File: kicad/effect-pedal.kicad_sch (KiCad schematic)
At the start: 50 parts, among them J4 Conn_01x08, J5 Conn_01x09, J6 Conn_01x09, J7 Conn_ARM_JTAG_SWD_10, J8 NJ3FD-V, J9 NJ3FD-V, P2 USB_C_Plug_USB2.0, SW1 RotaryEncoder_Switch, SW2 RotaryEncoder_Switch, SW3 RotaryEncoder_Switch, SW4 RotaryEncoder_Switch, SW5 SW_Push, SW6 SW_SPDT, U1 STM32H723ZGTx, U2 PCM5102A, Y1 Crystal

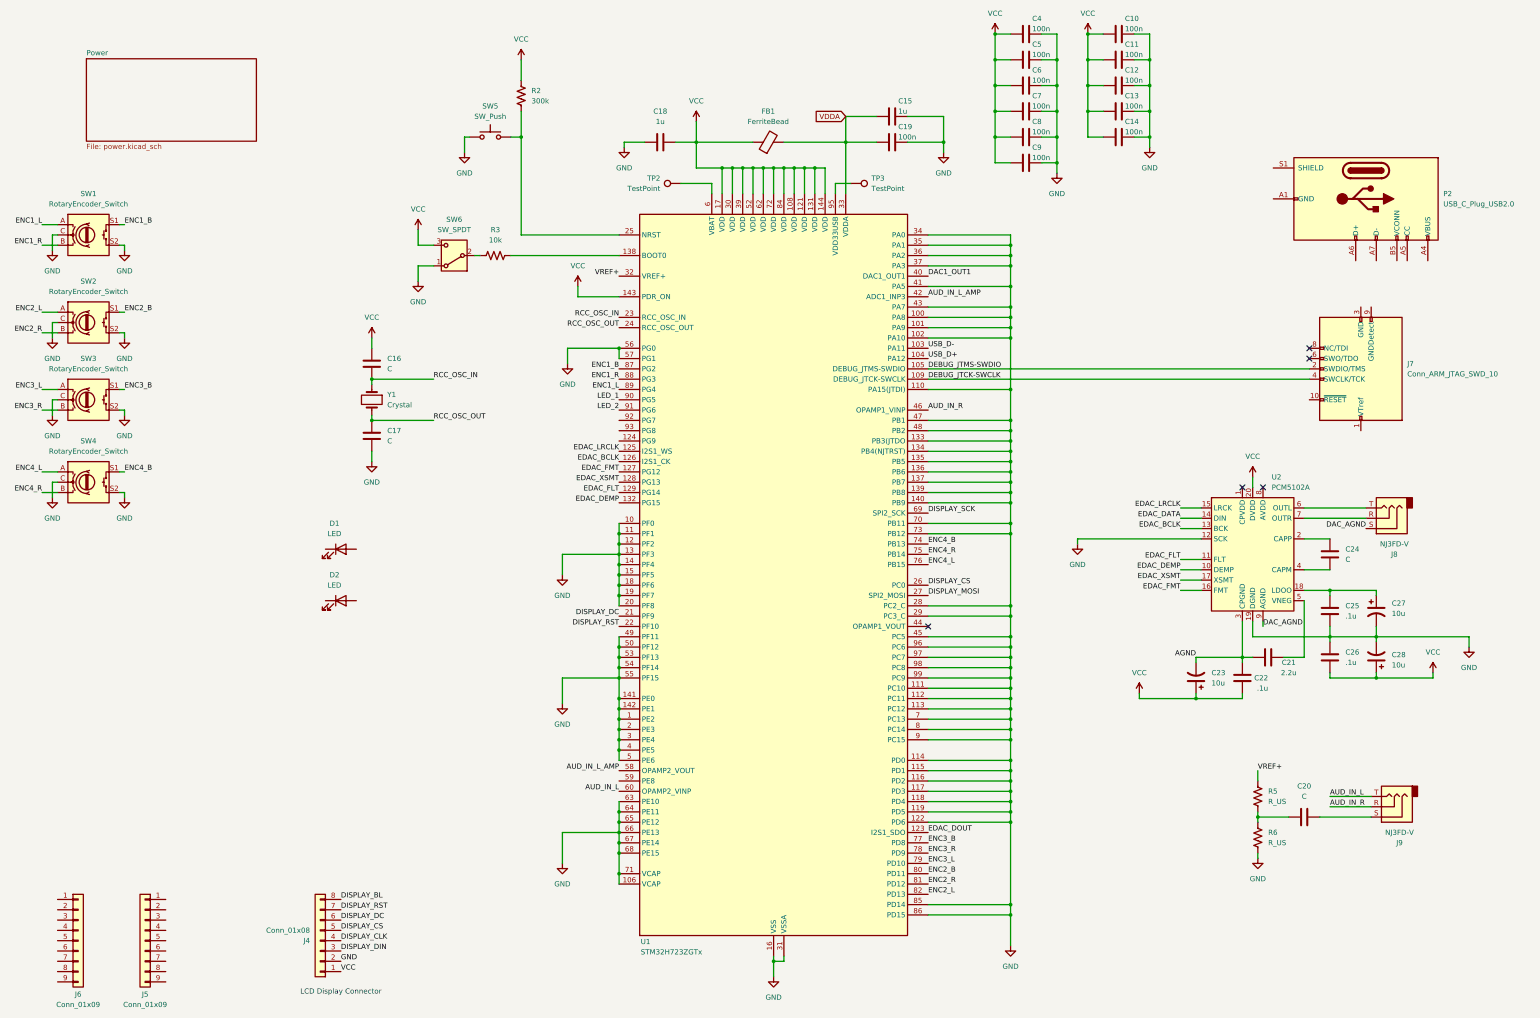
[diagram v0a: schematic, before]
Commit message: Clean up schematic
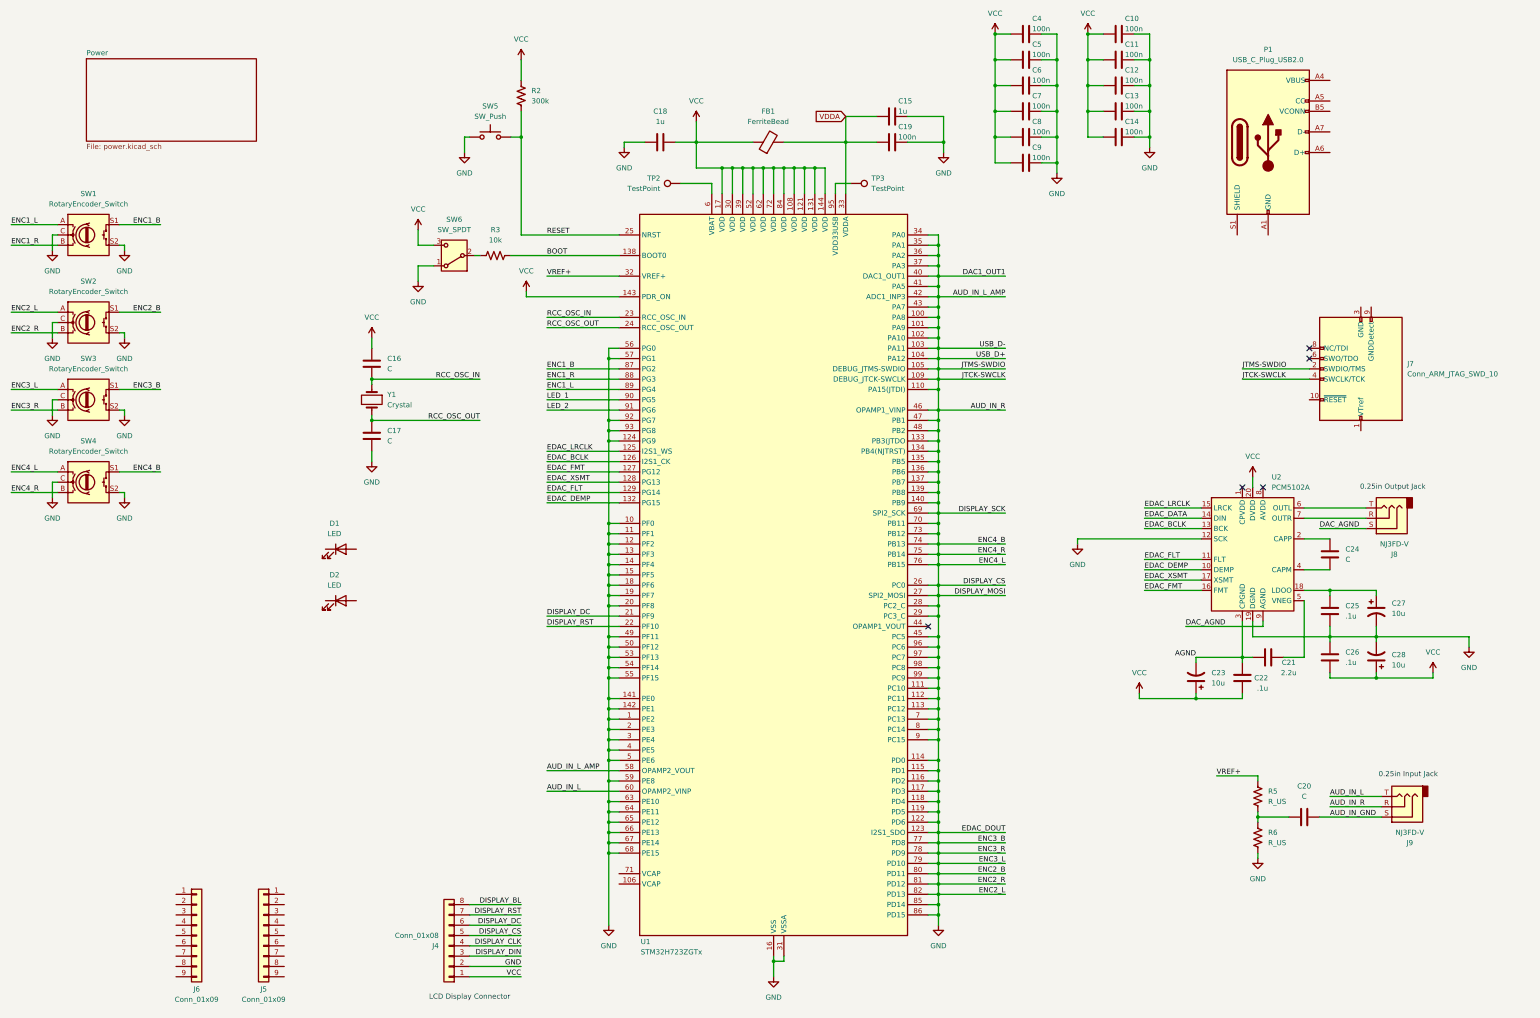
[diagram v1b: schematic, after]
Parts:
- removed P2: USB_C_Plug_USB2.0, symbol Connector:USB_C_Plug_USB2.0
- added P1: USB_C_Plug_USB2.0, symbol Connector:USB_C_Plug_USB2.0
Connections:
- net AUD_IN_L_AMP is gone; now on net GND: U1.42 (PA6), U1.58 (PE7)
- net AUD_IN_R is gone; now on net GND: J9.R, U1.46 (PB0)
- net DAC1_OUT1 is gone; now on net GND: U1.40 (PA4)
- net DEBUG_JTCK-SWCLK is gone; now on net GND: J7.4 (SWCLK/TCK), U1.109 (PA14(JTCK)
- net DEBUG_JTMS-SWDIO is gone; now on net GND: J7.2 (SWDIO/TMS), U1.105 (PA13(JTMS)
- net DISPLAY_CS is gone; now on net GND: J4.5 (Pin_5), U1.26 (PC0)
- net DISPLAY_MOSI is gone; now on net GND: U1.27 (PC1)
- net DISPLAY_SCK is gone; now on net GND: U1.69 (PB10)
- net EDAC_DOUT is gone; now on net GND: U1.123 (PD7)
- net ENC2_B is gone; now on net GND: SW2.S1, U1.80 (PD11)
- net ENC2_L is gone; now on net GND: SW2.A, U1.82 (PD13)
- net ENC2_R is gone; now on net GND: SW2.B, U1.81 (PD12)
- net ENC3_B is gone; now on net GND: SW3.S1, U1.77 (PD8)
- net ENC3_L is gone; now on net GND: SW3.A, U1.79 (PD10)
- net ENC3_R is gone; now on net GND: SW3.B, U1.78 (PD9)
- net ENC4_B is gone; now on net GND: SW4.S1, U1.74 (PB13)
- net ENC4_L is gone; now on net GND: SW4.A, U1.76 (PB15)
- net ENC4_R is gone; now on net GND: SW4.B, U1.75 (PB14)
- net USB_D+ is gone; now on net GND: U1.104 (PA12)
- net USB_D- is gone; now on net GND: U1.103 (PA11)
- net GND: now also U1.124 (PG9), U1.59 (PE8), U1.92 (PG7), U1.93 (PG8); no longer U1.106 (VCAP), U1.71 (VCAP)
- net AUD_IN_GND: now reaches C20.2, J9.S
- net BOOT: now reaches R3.1, U1.138 (BOOT0)
- net RESET: now reaches R2.2, SW5.2, U1.25 (NRST)
- new net: P1.A1 (GND), P1.A12 (GND), P1.B1 (GND), P1.B12 (GND)
- new net: P1.A4 (VBUS), P1.A9 (VBUS), P1.B4 (VBUS), P1.B9 (VBUS)
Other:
- note added: "0.25in Input Jack"
- note added: "0.25in Output Jack"
- moved on the sheet: J4, J5, J6, J9

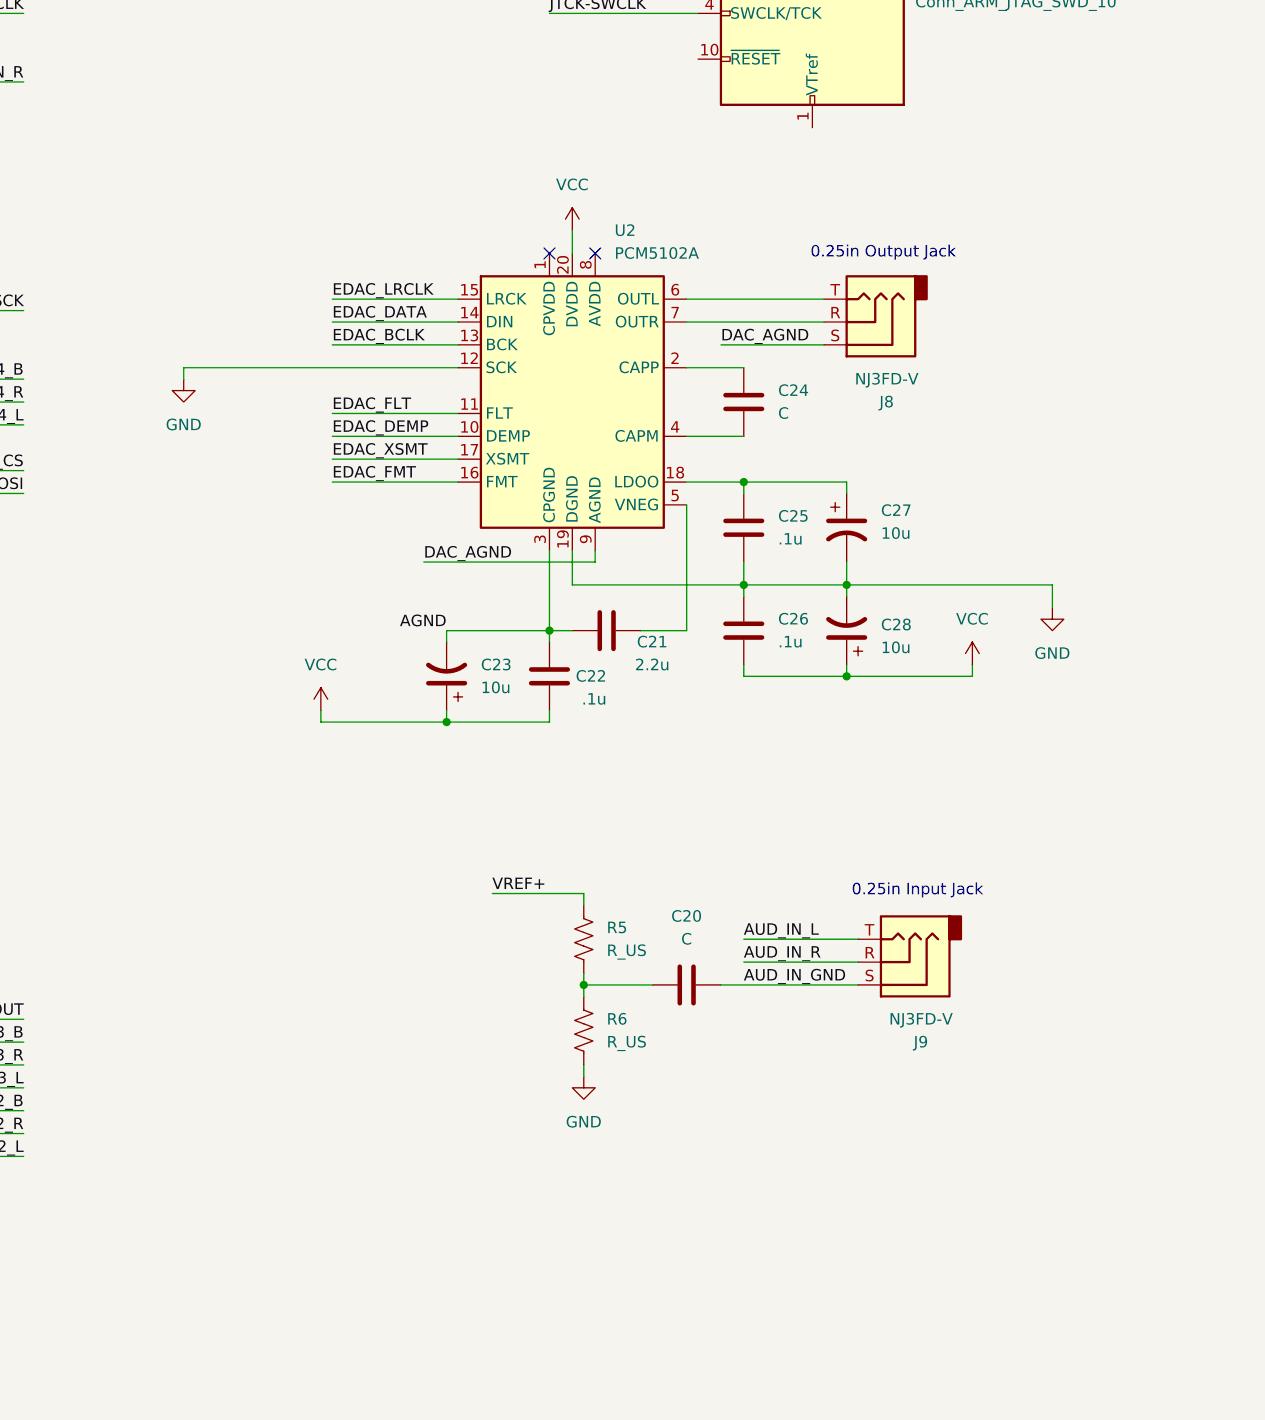
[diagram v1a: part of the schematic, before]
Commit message: Wiring on DAC pwr lines
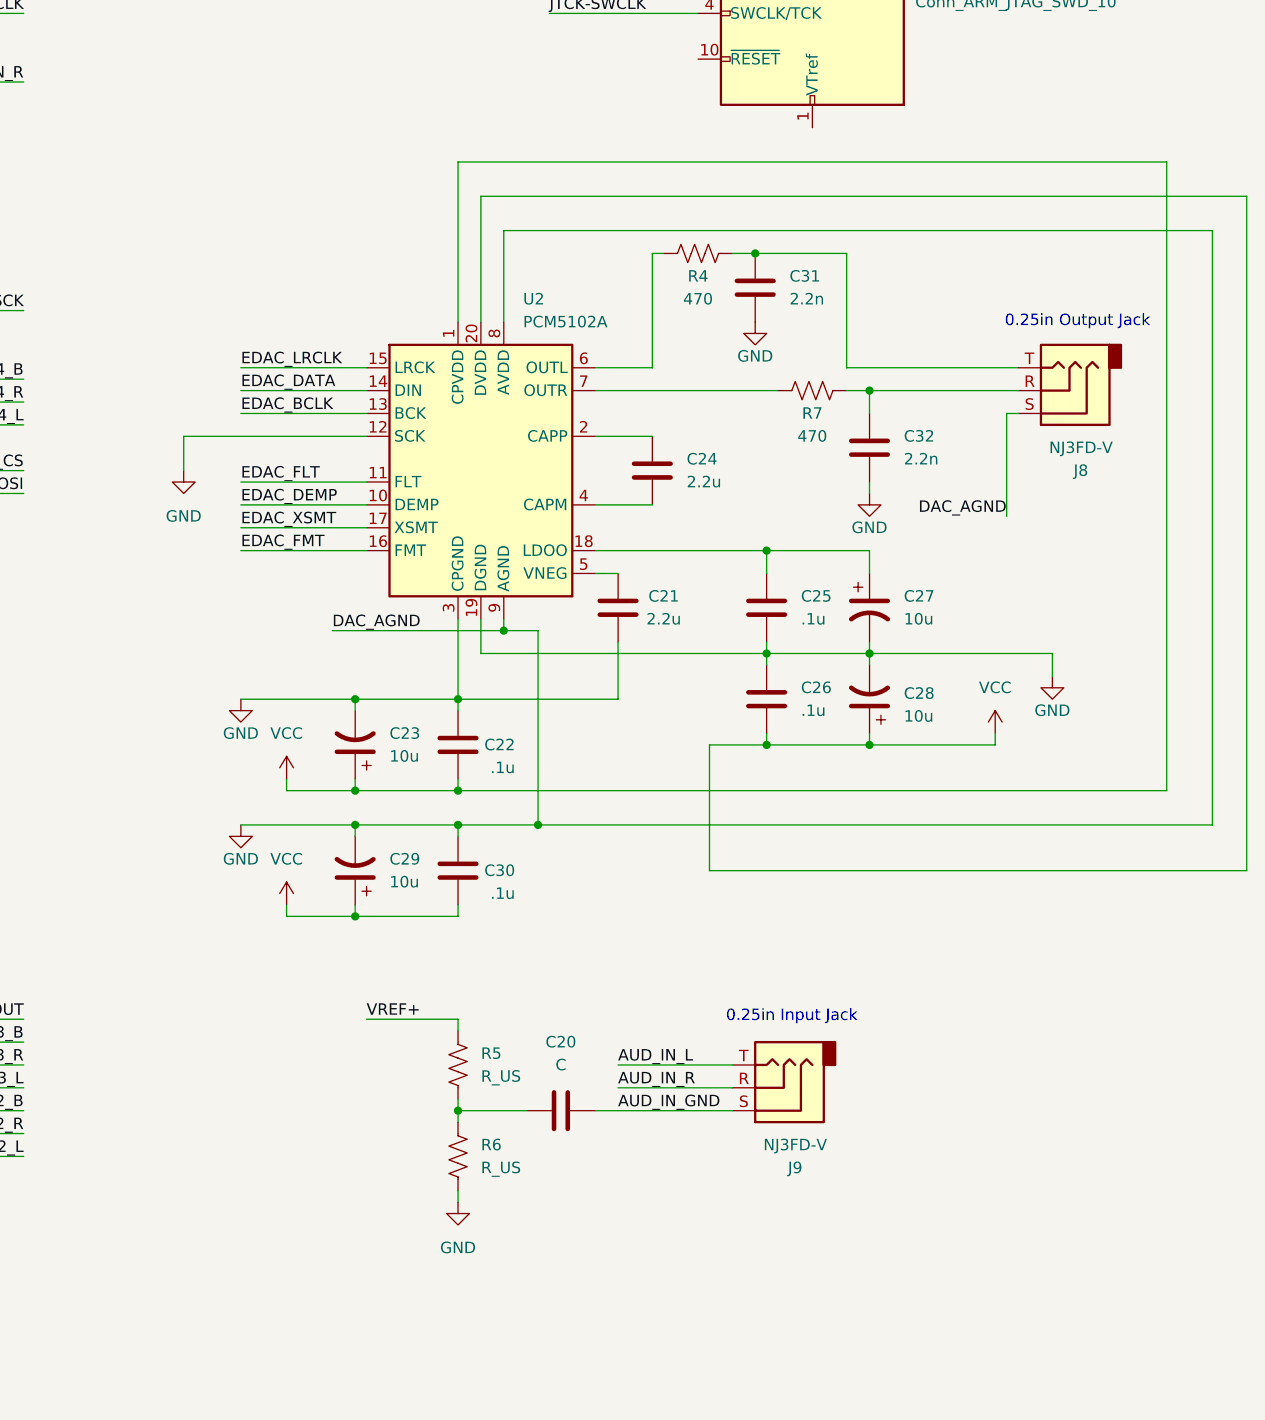
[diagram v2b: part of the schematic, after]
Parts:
- added C29: 10u, symbol Device:C_Polarized_US
- added C30: .1u, symbol Device:C
- added C31, C32: 2.2n, symbol Device:C
- added R4, R7: 470, symbol Device:R_US
- C24: value C -> 2.2u
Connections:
- net AGND is gone; now on net GND: C21.1, C22.2, C23.2, U2.3 (CPGND)
- net DAC_AGND is gone; now on net GND: J8.S, U2.9 (AGND)
- net GND: now also U2.8 (AVDD), C29.2, C30.2, C31.1, C32.1
- net VCC: now also U2.1 (CPVDD), C29.1, C30.1
- net at J8.R: now also C32.2, R7.2; no longer U2.7 (OUTR)
- net at J8.T: now also C31.2, R4.2; no longer U2.6 (OUTL)
- new net: R7.1, U2.7 (OUTR)
- new net: R4.1, U2.6 (OUTL)
- no-connect marks 5 -> 3
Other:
- moved on the sheet: C20, C21, C22, C23, C24, C25, C26, C27, C28, J8, J9, R5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

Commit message: usb stuff & display label changes
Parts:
- added C33: 2n, symbol Device:C
- added R8: 5.1k, symbol Device:R_US
- C20: value C -> 15u
- R5, R6: value R_US -> 3.3k
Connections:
- net DISPLAY_BL: now also U1.20 (PF8)
- net GND: now also J7.3 (GND), J7.5 (GND), P1.A1 (GND), P1.A12 (GND), P1.B1 (GND), P1.B12 (GND), C33.1, R8.2; no longer J4.5 (Pin_5), J7.2 (SWDIO/TMS), J7.4 (SWCLK/TCK), SW2.A, SW2.B, SW2.S1, SW3.A, SW3.B, SW3.S1, SW4.A, SW4.B, SW4.S1, U1.103 (PA11), U1.104 (PA12), U1.105 (PA13(JTMS), U1.109 (PA14(JTCK), U1.123 (PD7), U1.20 (PF8), U1.26 (PC0), U1.27 (PC1), U1.40 (PA4), U1.42 (PA6), U1.58 (PE7), U1.69 (PB10), U1.74 (PB13), U1.75 (PB14), U1.76 (PB15), U1.77 (PD8), U1.78 (PD9), U1.79 (PD10), U1.80 (PD11), U1.81 (PD12), U1.82 (PD13)
- net VCC: now also P1.A4 (VBUS), P1.A9 (VBUS), P1.B4 (VBUS), P1.B9 (VBUS)
- net at P1.A5 (CC): now also R8.1
- net USB_D+: now reaches P1.A6 (D+)
- net USB_D+: now also U1.104 (PA12)
- net USB_D-: now reaches P1.A7 (D-)
- net USB_D-: now also U1.103 (PA11)
- net at C20.1, R5.2, R6.1: now also C33.2
- net DISPLAY_CLK renamed DISPLAY_SCK
- net DISPLAY_SCK: now also U1.69 (PB10)
- net DISPLAY_DIN renamed DISPLAY_DATA
- net DISPLAY_DATA: now also U1.27 (PC1)
- new net AUD_IN_L_AMP: U1.42 (PA6), U1.58 (PE7)
- new net DAC1_OUT1: U1.40 (PA4)
- new net DISPLAY_CS: J4.5 (Pin_5), U1.26 (PC0)
- new net EDAC_DOUT: U1.123 (PD7)
- new net ENC2_B: SW2.S1, U1.80 (PD11)
- new net ENC2_L: SW2.A, U1.82 (PD13)
- new net ENC2_R: SW2.B, U1.81 (PD12)
- new net ENC3_B: SW3.S1, U1.77 (PD8)
- new net ENC3_L: SW3.A, U1.79 (PD10)
- new net ENC3_R: SW3.B, U1.78 (PD9)
- new net ENC4_B: SW4.S1, U1.74 (PB13)
- new net ENC4_L: SW4.A, U1.76 (PB15)
- new net ENC4_R: SW4.B, U1.75 (PB14)
- new net JTCK-SWCLK: J7.4 (SWCLK/TCK), U1.109 (PA14(JTCK)
- new net JTMS-SWDIO: J7.2 (SWDIO/TMS), U1.105 (PA13(JTMS)
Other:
- moved on the sheet: C10, C11, C12, C13, C14, C4, C5, C6, C7, C8, C9, J4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
